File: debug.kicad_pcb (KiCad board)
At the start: 2 copper layers, 58 parts, among them J1 USB_OTG, J2 CONN_01X04, J3 DEBUG, J4 TARGET_DEBUG, J5 MOLEX-MICRO-SD, J6 TARGET_UART, Q1 Q_NMOS_DGS, Q2 Q_NMOS_DGS, Q3 Q_NMOS_DGS, SW1 SPST, SW2 SPST, SW3 SPST, U1 74LVC125, U2 NLSX4373DR2G, U3 NLSX4373DR2G, U4 TC1262-33VDB, U5 MK20DX128VFM5, U6 MX25R1635F, U7 NLSX4373DR2G, Y1 32KHz, Y2 8MHz

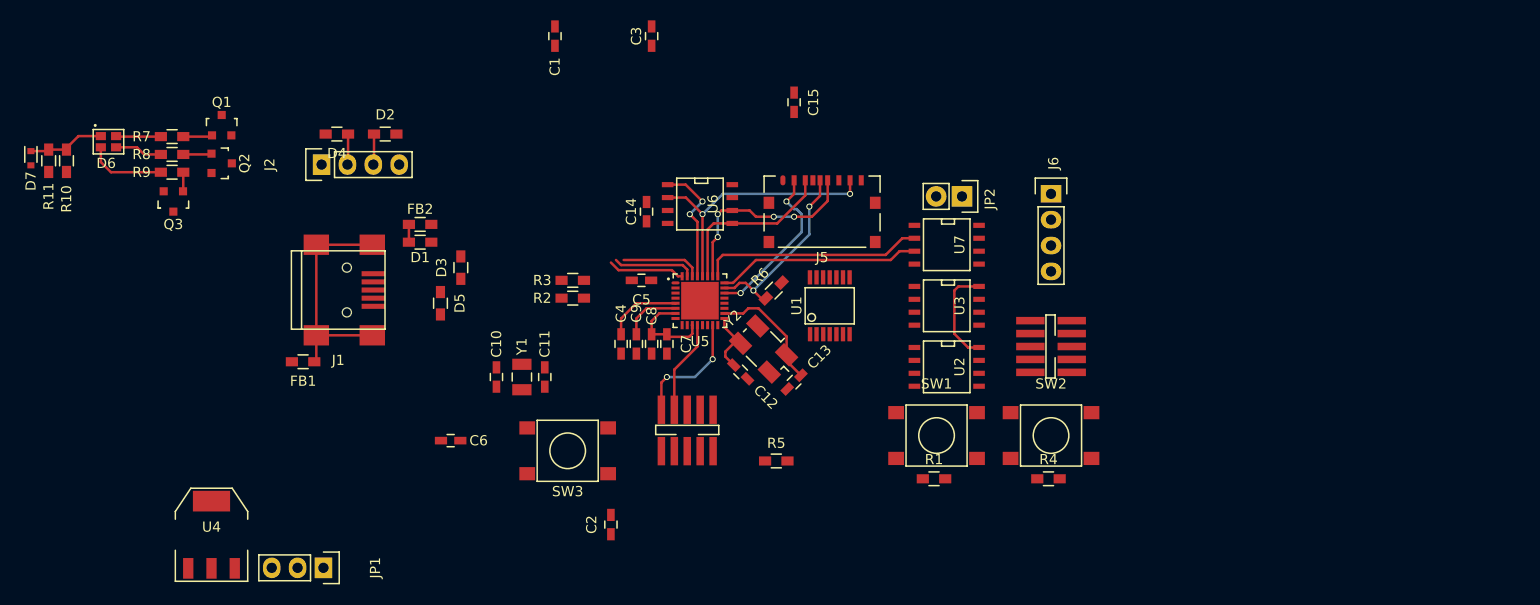
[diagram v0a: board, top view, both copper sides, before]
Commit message: replace large components with smaller ones
change to simple switching power supply
add board outline
simplify USB protection
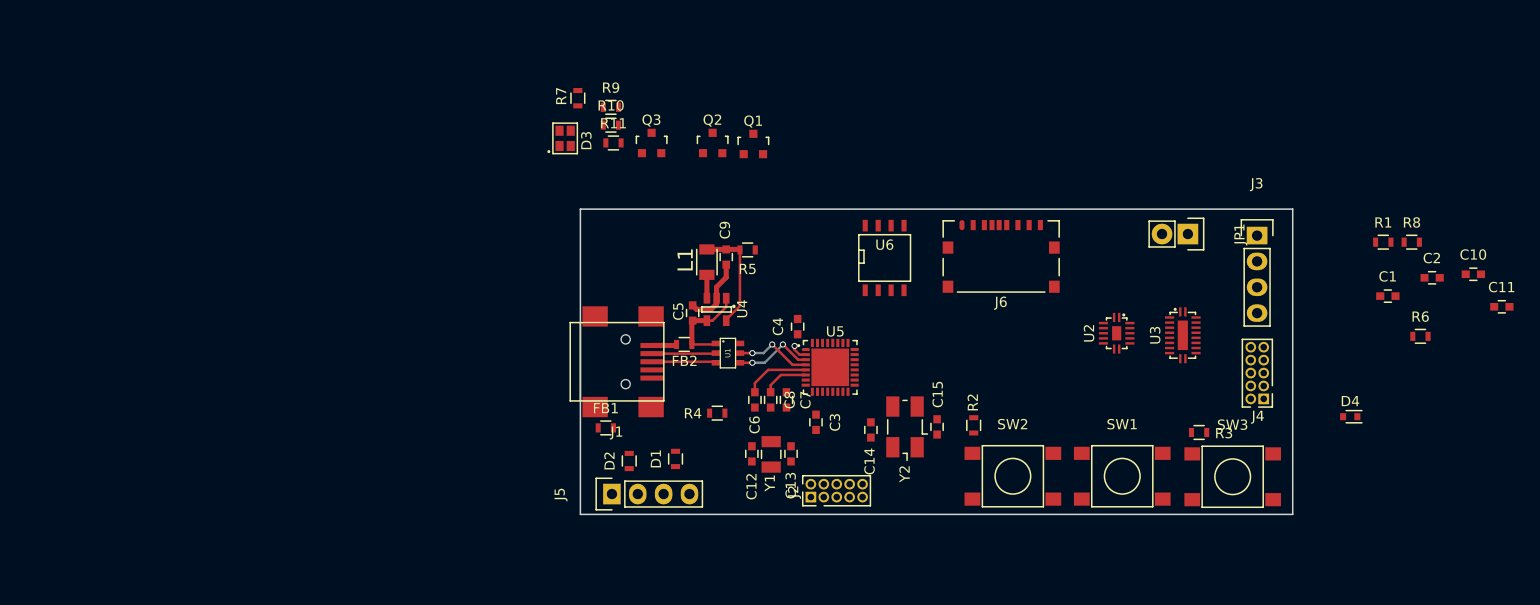
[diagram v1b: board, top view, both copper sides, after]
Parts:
- removed D5: TVS, footprints:D_0603
- removed D6: Led_RGB_CA, footprints:PLCC4
- removed D7: D_Schottky, Diodes_SMD:SOD-523
- removed JP2: Jumper_NO_Small, Pin_Headers:Pin_Header_Straight_1x02
- removed U7: NLSX4373DR2G, SMD_Packages:SOIC-8-N
- added L1: 2.2 uH, footprints:1008, F.Cu at (112.4, 105.2)
- C1, C3: value 1u -> 0.1u; footprint Capacitors_SMD:C_0603_HandSoldering -> Capacitors_SMD:C_0603
- C10: value C -> 0.1u; footprint Capacitors_SMD:C_0603_HandSoldering -> Capacitors_SMD:C_0603
- C11: value C -> 22u; footprint Capacitors_SMD:C_0603_HandSoldering -> Capacitors_SMD:C_0603
- C12, C13, C5, C7: footprint Capacitors_SMD:C_0603_HandSoldering -> Capacitors_SMD:C_0603
- C14: value 0.1u -> C; footprint Capacitors_SMD:C_0603_HandSoldering -> Capacitors_SMD:C_0603
- C15: value 22u -> C; footprint Capacitors_SMD:C_0603_HandSoldering -> Capacitors_SMD:C_0603
- C2: value 0.1u -> 10u; footprint Capacitors_SMD:C_0603_HandSoldering -> Capacitors_SMD:C_0603
- C4: value 2.2u -> 0.1u; footprint Capacitors_SMD:C_0603_HandSoldering -> Capacitors_SMD:C_0603
- C6, C8: value 0.1u -> 2.2u; footprint Capacitors_SMD:C_0603_HandSoldering -> Capacitors_SMD:C_0603
- C9: value 2.2u -> 10u; footprint Capacitors_SMD:C_0603_HandSoldering -> Capacitors_SMD:C_0603
- D1, D2: footprint footprints:D_0603 -> Resistors_SMD:R_0603
- D3: value TVS -> Led_RGB_CA; footprint footprints:D_0603 -> footprints:PLCC4
- D4: value TVS -> D_Schottky; footprint footprints:D_0603 -> Diodes_SMD:SOD-523
- FB1, FB2: footprint footprints:L_0603 -> Resistors_SMD:R_0603
- J2: value CONN_01X04 -> DEBUG; footprint Pin_Headers:Pin_Header_Straight_1x04 -> Pin_Headers:Pin_Header_Straight_2x05_Pitch1.27mm
- J3: value DEBUG -> TARGET_UART; footprint footprints:FTSH-105-01-L-DV-K -> Pin_Headers:Pin_Header_Straight_1x04
- J4: footprint footprints:FTSH-105-01-L-DV-K -> Pin_Headers:Pin_Header_Straight_2x05_Pitch1.27mm
- J5: value MOLEX-MICRO-SD -> CONN_01X04; footprint footprints:SD-105027-001 -> Pin_Headers:Pin_Header_Straight_1x04
- J6: value TARGET_UART -> MOLEX-MICRO-SD; footprint Pin_Headers:Pin_Header_Straight_1x04 -> footprints:SD-105027-001
- JP1: value JUMPER3 -> Jumper_NO_Small; footprint Pin_Headers:Pin_Header_Straight_1x03 -> Pin_Headers:Pin_Header_Straight_1x02
- R1, R10, R11, R6, R7, R8, R9: footprint Resistors_SMD:R_0603_HandSoldering -> Resistors_SMD:R_0603
- R2, R3: value 33 -> 10k; footprint Resistors_SMD:R_0603_HandSoldering -> Resistors_SMD:R_0603
- R4, R5: value 10k -> 0; footprint Resistors_SMD:R_0603_HandSoldering -> Resistors_SMD:R_0603
- U1: value 74LVC125 -> STF202-22; footprint SMD_Packages:SSOP-14 -> footprints:SOT457
- U2: value NLSX4373DR2G -> 74LVC125; footprint SMD_Packages:SOIC-8-N -> footprints:DHVQFN14
- U3: value NLSX4373DR2G -> FXMA108BQX; footprint SMD_Packages:SOIC-8-N -> footprints:DQFN20
- U4: value TC1262-33VDB -> PAM2301; footprint TO_SOT_Packages_SMD:SOT-223 -> TO_SOT_Packages_SMD:SOT-23-5
- moved R8 122.1 mm to (181.7, 103.2)
- moved D4 103.4 mm to (175.7, 120.4), turned to 0 degrees
- moved C10 96.5 mm to (187.8, 106.4), turned to 0 degrees
- moved C11 94.3 mm to (190.6, 109.6), turned to 0 degrees
- moved JP1 91.1 mm to (159.7, 102.5)
- moved C1 85.7 mm to (179.3, 108.5), turned to 0 degrees
- moved C2 84.3 mm to (183.7, 106.8), turned to 0 degrees
- moved SW3 65.4 mm to (164.1, 126.3)
- moved R6 63.7 mm to (182.6, 112.5), turned to 0 degrees
- moved R3 63.3 mm to (160.8, 122.0)
- moved J3 59.2 mm to (166.5, 102.6)
- moved J2 58.1 mm to (122.7, 128.3)
- moved R11 55.5 mm to (103.2, 93.5), turned to 0 degrees
- moved U4 54.3 mm to (113.4, 109.9), turned to 270 degrees
- moved R10 53.6 mm to (103.0, 91.8), turned to 0 degrees
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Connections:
- C1 pad 1: +5V -> VCC
- C10 pad 1: XTAL32 -> VCC
- C11 pad 1: EXTAL32 -> VCC
- C12 pad 1: XTAL -> XTAL32
- C13 pad 1: EXTAL -> EXTAL32
- C14 pad 1: VCC -> XTAL
- C15 pad 1: VCC -> EXTAL
- C3 pad 1: Net-(C3-Pad1) -> VCC
- C4 pad 1: Net-(C4-Pad1) -> VCC
- C5 pad 1: VCC -> +5V
- C6 pad 1: VCC -> Net-(C6-Pad1)
- C8 pad 1: VCC -> +5V
- C9 pad 1: +5V -> Net-(C9-Pad1)
- D1 pad 1: Net-(D1-Pad1) -> UART0_TX
- D2 pad 1: UART0_TX -> UART0_RX
- D3 pad 1: /USB_D- -> Net-(D3-Pad1)
- D3 pad 2: GND -> Net-(D3-Pad2)
- D4 pad 1: UART0_RX -> Net-(D3-Pad1)
- D4 pad 2: GND -> VCC
- FB2 pad 1: Net-(D1-Pad1) -> Net-(FB2-Pad1)
- J1 pad 1: Net-(D1-Pad1) -> Net-(FB2-Pad1)
- J2 pad 2: UART0_RX -> SWD_DIO
- J2 pad 3: UART0_TX -> GND
- J2 pad 4: GND -> SWD_CLK
- J3 pad 1: VCC -> VCOM
- J3 pad 2: SWD_DIO -> Net-(J3-Pad2)
- J3 pad 3: GND -> Net-(J3-Pad3)
- J3 pad 4: SWD_CLK -> GND
- JP1 pad 1: Net-(C4-Pad1) -> VCOM
- R10 pad 2: Net-(D6-Pad1) -> Net-(D3-Pad1)
- R11 pad 2: Net-(D6-Pad1) -> Net-(D3-Pad1)
- R2 pad 1: /USB_D- -> VCC
- R2 pad 2: USB2_D- -> RESET
- R3 pad 1: /USB_D+ -> VCOM
- R3 pad 2: USB2_D+ -> /TARGET_RESET
- R4 pad 1: VCOM -> Net-(C6-Pad1)
- R4 pad 2: /TARGET_RESET -> VCC
- R5 pad 2: RESET -> Net-(C9-Pad1)
- R7 pad 1: Net-(D6-Pad2) -> Net-(D3-Pad2)
- R8 pad 1: Net-(D6-Pad3) -> Net-(D3-Pad3)
- R9 pad 1: Net-(D6-Pad4) -> Net-(D3-Pad4)
- SW2 pad 1: /TARGET_RESET -> RESET
- SW3 pad 1: RESET -> /TARGET_RESET
- U1 pad 1: TARGET_SWD_OE -> +5V
- U1 pad 2: SPI_MOSI -> /USB_D-
- U1 pad 3: Net-(U1-Pad3) -> /USB_D+
- U1 pad 4: TARGET_SWD_OE -> USB2_D+
- U1 pad 5: Net-(U1-Pad3) -> USB2_D-
- U1 pad 6: SPI_MISO -> GND
- U2 pad 1: VCC -> TARGET_SWD_OE
- U2 pad 2: Net-(U1-Pad3) -> SPI_MOSI
- U2 pad 4: GND -> TARGET_SWD_OE
- U2 pad 5: GND -> Net-(U2-Pad3)
- U2 pad 6: Net-(U2-Pad6) -> SPI_MISO
- U2 pad 7: /TARGET_SWDIO -> GND
- U2 pad 8: VCOM -> Net-(U2-Pad8)
- U3 pad 2: Net-(U1-Pad8) -> UART1_TX
- U3 pad 3: RESET_OUT -> UART1_RX
- U3 pad 4: GND -> Net-(U2-Pad3)
- U3 pad 5: GND -> Net-(U2-Pad8)
- U3 pad 6: /TARGET_RESET -> RESET_OUT
- U3 pad 7: /TARGET_SWD_CLK -> Net-(U3-Pad7)
- U3 pad 8: VCOM -> Net-(U3-Pad8)
- U4 pad 3: Net-(C3-Pad1) -> Net-(L1-Pad1)
- U4 pad 4: GND -> +5V
- U5 pad 5: Net-(C4-Pad1) -> Net-(C6-Pad1)
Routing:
- net SPI_MISO: track 26.9 -> 0.00 mm, vias 2 -> 0
- net Net-(FB1-Pad1): track 22.6 -> 0.00 mm
- net UART1_TX: track 21.8 -> 0.00 mm
- net SPI_CLK: track 20.2 -> 0.00 mm, vias 4 -> 0
- net UART1_RX: track 20.0 -> 0.00 mm
- net SD_SWITCH: track 18.5 -> 0.00 mm, vias 2 -> 0
- net SPI_MOSI: track 17.1 -> 0.00 mm
- net SD_CS: track 16.2 -> 0.00 mm, vias 2 -> 0
- net FLASH_CS: track 12.3 -> 0.00 mm, vias 2 -> 0
- net SWD_DIO: track 12.0 -> 0.00 mm, vias 2 -> 0
- net EXTAL: track 11.9 -> 0.00 mm
- net Net-(C9-Pad1): track 0.00 -> 10.8 mm
- net SWD_CLK: track 9.25 -> 0.00 mm
- net VCOM: track 9.21 -> 0.00 mm
- net VCC: track 8.98 -> 0.00 mm
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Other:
- board outline added: 70 x 30 mm

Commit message: progress
simplify LEDs
fix ferrite bead on 5v
lots of routing I'll have to redo anyway later
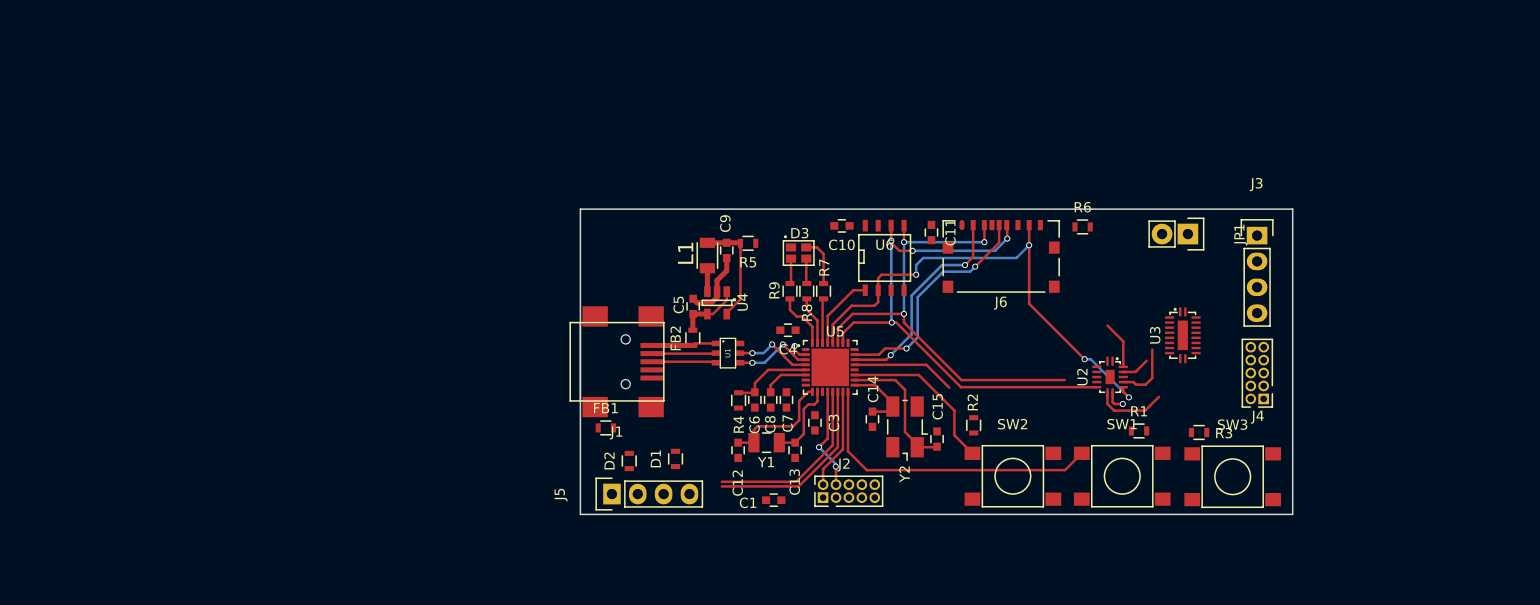
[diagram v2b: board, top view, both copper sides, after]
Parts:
- removed C2: 10u, Capacitors_SMD:C_0603
- removed D4: D_Schottky, Diodes_SMD:SOD-523
- removed Q1, Q2, Q3: Q_NMOS_DGS, TO_SOT_Packages_SMD:SOT-23
- removed R10, R11: 0, Resistors_SMD:R_0603
- moved C1 63.6 mm to (119.0, 128.6), turned to 180 degrees
- moved C10 62.2 mm to (125.7, 101.7), turned to 180 degrees
- moved R8 59.6 mm to (122.2, 108.1), turned to 270 degrees
- moved C11 56.5 mm to (134.5, 102.3), turned to 270 degrees
- moved R6 34.9 mm to (149.3, 101.8)
- moved R7 30.7 mm to (123.9, 108.1)
- moved R1 30.3 mm to (154.9, 121.8)
- moved D3 25.6 mm to (121.4, 104.3), turned to 180 degrees
- moved R9 25.2 mm to (120.6, 108.1), turned to 270 degrees
- moved U2 4.35 mm to (152.1, 116.5)
- moved R4 2.44 mm to (115.5, 118.8), turned to 270 degrees
- moved C12 1.39 mm to (115.5, 123.7)
- moved Y1 1.23 mm to (118.3, 123.0), turned to 0 degrees
- moved J2 1.20 mm to (123.8, 128.3)
- moved C15 1.20 mm to (135.1, 122.6)
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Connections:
- D3 pad 1: Net-(D3-Pad1) -> VCC
- FB2 pad 1: Net-(FB2-Pad1) -> +5V
- FB2 pad 2: +5V -> Net-(FB2-Pad2)
- J1 pad 1: Net-(FB2-Pad1) -> Net-(FB2-Pad2)
- R7 pad 2: Net-(Q1-Pad1) -> LED_R
- R8 pad 2: Net-(Q2-Pad1) -> LED_G
- R9 pad 2: Net-(Q3-Pad1) -> LED_B
- U1 pad 1: +5V -> Net-(FB2-Pad2)
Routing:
- net SPI_CLK: track 0.00 -> 52.3 mm, vias 0 -> 4
- net SPI_MOSI: track 0.00 -> 50.4 mm, vias 0 -> 3
- net SPI_MISO: track 0.00 -> 48.8 mm, vias 0 -> 4
- net PROGRAM: track 0.00 -> 30.3 mm
- net SD_SWITCH: track 0.00 -> 22.8 mm, vias 0 -> 2
- net SD_CS: track 0.00 -> 21.2 mm, vias 0 -> 2
- net UART0_TX: track 0.00 -> 18.4 mm
- net UART0_RX: track 0.00 -> 17.6 mm
- net RESET: track 0.00 -> 16.2 mm
- net EXTAL: track 0.00 -> 13.3 mm
- net XTAL32: track 0.00 -> 11.2 mm
- net RESET_OUT: track 0.00 -> 10.2 mm
- net SWD_CLK: track 0.00 -> 10.2 mm, vias 0 -> 2
- net SWD_DIO: track 0.00 -> 9.94 mm
- net Net-(U2-Pad3): track 0.00 -> 8.83 mm
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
